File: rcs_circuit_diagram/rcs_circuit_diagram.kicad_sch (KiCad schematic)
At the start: 50 parts, among them J1 Conn_01x06_Pin, J11 Conn_01x02_Pin, J13 Conn_01x02_Pin, J15 Conn_01x02_Pin, J3 Conn_01x02_Pin, J5 Conn_01x02_Pin, J6 Conn_01x02_Pin, J7 Conn_01x02_Pin, J9 Conn_01x02_Pin, U1 LM2596S-5

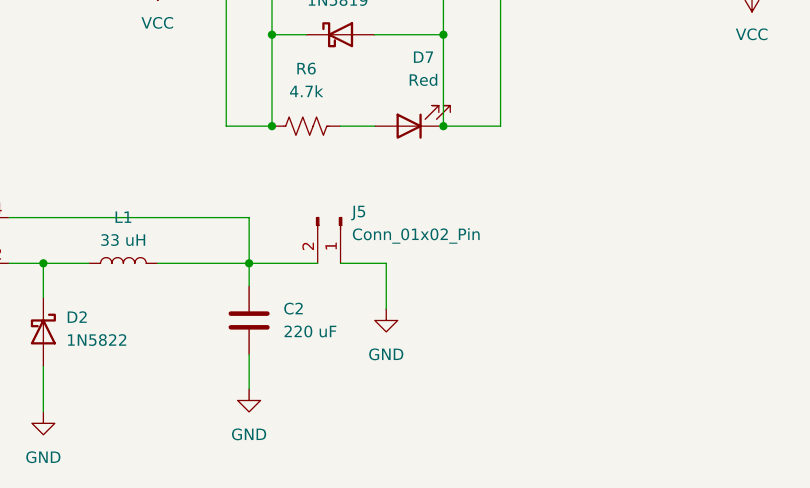
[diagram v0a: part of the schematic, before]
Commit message: Fixed power connection
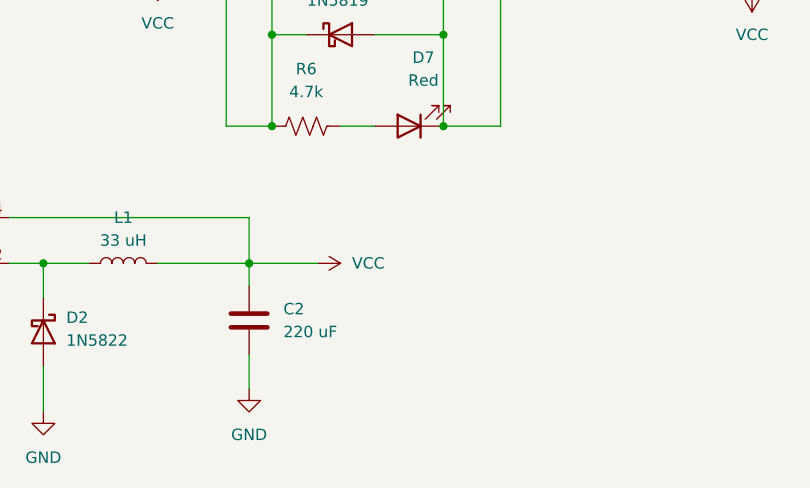
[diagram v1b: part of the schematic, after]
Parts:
- removed J5: Conn_01x02_Pin, symbol Connector:Conn_01x02_Pin
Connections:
- net VCC: now also C2.1, L1.2, U1.4 (FB)
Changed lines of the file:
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@@
-    (stroke (width 0) (type default))
-  )
-  (wire (pts (xy 223.52 229.87) (xy 223.52 234.95))
     (stroke (width 0) (type default))
   )
@@
   )
   (wire (pts (xy 292.1 93.98) (xy 364.49 93.98))
-    (stroke (width 0) (type default))
-  )
-  (wire (pts (xy 218.44 229.87) (xy 223.52 229.87))
     (stroke (width 0) (type default))
   )
@@
     )
   )
-  (symbol (lib_id "power:GND") (at 223.52 234.95 0) (unit 1)
-    (in_bom yes) (on_board yes) (dnp no) (fields_autoplaced)
-    (property "Reference" "#PWR013" (at 223.52 241.3 0)
-      (effects (font (size 1.27 1.27)) hide)
-    )
-    (property "Value" "GND" (at 223.52 240.03 0)
-      (effects (font (size 1.27 1.27)))
-    )
-    (property "Footprint" "" (at 223.52 234.95 0)
-      (effects (font (size 1.27 1.27)) hide)
-    )
-    (property "Datasheet" "" (at 223.52 234.95 0)
-      (effects (font (size 1.27 1.27)) hide)
-    )
-    (pin "1")
-    (instances
-      (project "rcs_circuit_diagram"
-        (path "/c5cfa2cd-8217-4cc7-84bd-4a928cc21c13"
-          (reference "#PWR013") (unit 1)
-        )
-      )
-    )
-  )
   (symbol (lib_id "power:GND") (at 207.01 110.49 0) (unit 1)
     (in_bom yes) (on_board yes) (dnp no) (fields_autoplaced)
@@
         (path "/c5cfa2cd-8217-4cc7-84bd-4a928cc21c13"
           (reference "#PWR032") (unit 1)
+        )
+      )
+    )
+  )
+  (symbol (lib_id "power:VCC") (at 215.9 229.87 270) (unit 1)
+    (in_bom yes) (on_board yes) (dnp no) (fields_autoplaced)
+    (property "Reference" "#PWR013" (at 212.09 229.87 0)
+      (effects (font (size 1.27 1.27)) hide)
+    )
+    (property "Value" "VCC" (at 219.71 229.87 90)
+      (effects (font (size 1.27 1.27)) (justify left))
+    )
+    (property "Footprint" "" (at 215.9 229.87 0)
+      (effects (font (size 1.27 1.27)) hide)
+    )
+    (property "Datasheet" "" (at 215.9 229.87 0)
+      (effects (font (size 1.27 1.27)) hide)
+    )
+    (pin "1")
+    (instances
+      (project "rcs_circuit_diagram"
+        (path "/c5cfa2cd-8217-4cc7-84bd-4a928cc21c13"
+          (reference "#PWR013") (unit 1)
         )
       )
@@
         )
       )
-    )
-  )
-  (symbol (lib_id "Connector:Conn_01x02_Pin") (at 218.44 224.79 270) (unit 1)
-    (in_bom yes) (on_board yes) (dnp no) (fields_autoplaced)
-    (property "Reference" "J5" (at 219.71 224.155 90)
-      (effects (font (size 1.27 1.27)) (justify left))
-    )
-    (property "Value" "Conn_01x02_Pin" (at 219.71 226.695 90)
-      (effects (font (size 1.27 1.27)) (justify left))
-    )
-    (property "Footprint" "" (at 218.44 224.79 0)
-      (effects (font (size 1.27 1.27)) hide)
-    )
-    (property "Datasheet" "~" (at 218.44 224.79 0)
-      (effects (font (size 1.27 1.27)) hide)
-    )
-    (pin "1")
-    (pin "2")
-    (instances
-      (project "rcs_circuit_diagram"
-        (path "/c5cfa2cd-8217-4cc7-84bd-4a928cc21c13"
-          (reference "J5") (unit 1)
-        )
-      )

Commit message: Update rcs_circuit_diagram.kicad_sch
Added footprints
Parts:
- C1, C2: footprint (none) -> Capacitor_SMD:C_0402_1005Metric
- D1, D3, D4, D5, D6, D7: footprint (none) -> LED_SMD:LED_0603_1608Metric
- J1: footprint (none) -> Connector_PinHeader_2.54mm:PinHeader_1x06_P2.54mm_Vertical
- J11, J13, J15, J3, J6, J7, J9: footprint (none) -> Connector_PinHeader_2.54mm:PinHeader_1x02_P2.54mm_Vertical
- L1: footprint (none) -> Inductor_SMD:L_0603_1608Metric
- R1, R2, R3, R4, R5, R6: footprint (none) -> Resistor_SMD:R_0402_1005Metric
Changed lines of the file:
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@@
       (effects (font (size 1.27 1.27)))
     )
-    (property "Footprint" "" (at 214.884 213.614 90)
+    (property "Footprint" "Resistor_SMD:R_0402_1005Metric" (at 214.884 213.614 90)
       (effects (font (size 1.27 1.27)) hide)
     )
@@
       (effects (font (size 1.27 1.27)))
     )
-    (property "Footprint" "" (at 105.664 209.804 90)
+    (property "Footprint" "Resistor_SMD:R_0402_1005Metric" (at 105.664 209.804 90)
       (effects (font (size 1.27 1.27)) hide)
     )
@@
       (effects (font (size 1.27 1.27)) (justify left))
     )
-    (property "Footprint" "" (at 144.4752 236.22 0)
+    (property "Footprint" "Capacitor_SMD:C_0402_1005Metric" (at 144.4752 236.22 0)
       (effects (font (size 1.27 1.27)) hide)
     )
@@
       (effects (font (size 1.27 1.27)) (justify left))
     )
-    (property "Footprint" "" (at 284.48 190.5 0)
+    (property "Footprint" "Connector_PinHeader_2.54mm:PinHeader_1x02_P2.54mm_Vertical" (at 284.48 190.5 0)
       (effects (font (size 1.27 1.27)) hide)
     )
@@
       (effects (font (size 1.27 1.27)))
     )
-    (property "Footprint" "" (at 349.25 148.59 0)
+    (property "Footprint" "LED_SMD:LED_0603_1608Metric" (at 349.25 148.59 0)
       (effects (font (size 1.27 1.27)) hide)
     )
@@
       (effects (font (size 1.27 1.27)) (justify left))
     )
-    (property "Footprint" "" (at 218.44 189.23 0)
+    (property "Footprint" "Connector_PinHeader_2.54mm:PinHeader_1x02_P2.54mm_Vertical" (at 218.44 189.23 0)
       (effects (font (size 1.27 1.27)) hide)
     )
@@
       (effects (font (size 1.27 1.27)))
     )
-    (property "Footprint" "" (at 226.06 214.63 0)
+    (property "Footprint" "LED_SMD:LED_0603_1608Metric" (at 226.06 214.63 0)
       (effects (font (size 1.27 1.27)) hide)
     )
@@
       (effects (font (size 1.27 1.27)))
     )
-    (property "Footprint" "" (at 120.65 210.82 0)
+    (property "Footprint" "LED_SMD:LED_0603_1608Metric" (at 120.65 210.82 0)
       (effects (font (size 1.27 1.27)) hide)
     )
@@
       (effects (font (size 1.27 1.27)))
     )
-    (property "Footprint" "" (at 212.344 147.574 90)
+    (property "Footprint" "Resistor_SMD:R_0402_1005Metric" (at 212.344 147.574 90)
       (effects (font (size 1.27 1.27)) hide)
     )
@@
       (effects (font (size 1.27 1.27)))
     )
-    (property "Footprint" "" (at 194.31 229.87 0)
+    (property "Footprint" "Inductor_SMD:L_0603_1608Metric" (at 194.31 229.87 0)
       (effects (font (size 1.27 1.27)) hide)
     )
@@
       (effects (font (size 1.27 1.27)))
     )
-    (property "Footprint" "" (at 119.634 143.764 90)
+    (property "Footprint" "Resistor_SMD:R_0402_1005Metric" (at 119.634 143.764 90)
       (effects (font (size 1.27 1.27)) hide)
     )
@@
       (effects (font (size 1.27 1.27)))
     )
-    (property "Footprint" "" (at 41.91 125.73 0)
+    (property "Footprint" "Connector_PinHeader_2.54mm:PinHeader_1x06_P2.54mm_Vertical" (at 41.91 125.73 0)
       (effects (font (size 1.27 1.27)) hide)
     )
@@
       (effects (font (size 1.27 1.27)))
     )
-    (property "Footprint" "" (at 43.18 144.78 0)
+    (property "Footprint" "Connector_PinHeader_2.54mm:PinHeader_1x02_P2.54mm_Vertical" (at 43.18 144.78 0)
       (effects (font (size 1.27 1.27)) hide)
     )
@@
       (effects (font (size 1.27 1.27)))
     )
-    (property "Footprint" "" (at 223.52 148.59 0)
+    (property "Footprint" "LED_SMD:LED_0603_1608Metric" (at 223.52 148.59 0)
       (effects (font (size 1.27 1.27)) hide)
     )
@@
       (effects (font (size 1.27 1.27)))
     )
-    (property "Footprint" "" (at 280.924 214.884 90)
+    (property "Footprint" "Resistor_SMD:R_0402_1005Metric" (at 280.924 214.884 90)
       (effects (font (size 1.27 1.27)) hide)
     )
@@
       (effects (font (size 1.27 1.27)) (justify left))
     )
-    (property "Footprint" "" (at 209.2452 240.03 0)
+    (property "Footprint" "Capacitor_SMD:C_0402_1005Metric" (at 209.2452 240.03 0)
       (effects (font (size 1.27 1.27)) hide)
     )
@@
       (effects (font (size 1.27 1.27)) (justify left))
     )
-    (property "Footprint" "" (at 113.03 185.42 0)
+    (property "Footprint" "Connector_PinHeader_2.54mm:PinHeader_1x02_P2.54mm_Vertical" (at 113.03 185.42 0)
       (effects (font (size 1.27 1.27)) hide)
     )
@@
       (effects (font (size 1.27 1.27)))
     )
-    (property "Footprint" "" (at 338.074 147.574 90)
+    (property "Footprint" "Resistor_SMD:R_0402_1005Metric" (at 338.074 147.574 90)
       (effects (font (size 1.27 1.27)) hide)
     )
@@
       (effects (font (size 1.27 1.27)))
     )
-    (property "Footprint" "" (at 130.81 144.78 0)
+    (property "Footprint" "LED_SMD:LED_0603_1608Metric" (at 130.81 144.78 0)
       (effects (font (size 1.27 1.27)) hide)
     )
@@
       (effects (font (size 1.27 1.27)) (justify left))
     )
-    (property "Footprint" "" (at 215.9 123.19 0)
+    (property "Footprint" "Connector_PinHeader_2.54mm:PinHeader_1x02_P2.54mm_Vertical" (at 215.9 123.19 0)
       (effects (font (size 1.27 1.27)) hide)
     )
@@
       (effects (font (size 1.27 1.27)) (justify left))
     )
-    (property "Footprint" "" (at 341.63 123.19 0)
+    (property "Footprint" "Connector_PinHeader_2.54mm:PinHeader_1x02_P2.54mm_Vertical" (at 341.63 123.19 0)
       (effects (font (size 1.27 1.27)) hide)
     )
@@
       (effects (font (size 1.27 1.27)))
     )
-    (property "Footprint" "" (at 292.1 215.9 0)
+    (property "Footprint" "LED_SMD:LED_0603_1608Metric" (at 292.1 215.9 0)
       (effects (font (size 1.27 1.27)) hide)
     )
@@
       (effects (font (size 1.27 1.27)) (justify left))
     )
-    (property "Footprint" "" (at 123.19 119.38 0)
-      (effects (font (size 1.27 1.27)) hide)
-    )
+    (property "Footprint" "Connector_PinHeader_2.54mm:PinHeader_1x02_P2.54mm_Vertical" (at 123.19 119.38 0)
+      (effects (font (size 1.27 1.27)) hide)
+    )

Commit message: Updated footprints, changed layout of components
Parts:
- removed C1: 680 uF, Capacitor_SMD:C_0402_1005Metric, symbol Device:C
- added C3: C_Polarized, Capacitor_THT:CP_Radial_D10.0mm_P2.50mm, symbol Device:C_Polarized
- MOSFET1, MOSFET10, MOSFET11, MOSFET12, MOSFET13, MOSFET14, MOSFET15, MOSFET16, MOSFET17, MOSFET18, MOSFET2, MOSFET3, MOSFET4, MOSFET5, MOSFET6, MOSFET7, MOSFET8, MOSFET9: footprint Package_TO_SOT_THT:TO-220-3_Vertical -> Package_TO_SOT_THT:TO-220-3_Horizontal_TabDown
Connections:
- net GND: now also C3.2
- net VCC: now also C3.1
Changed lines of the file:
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@@
       (effects (font (size 1.27 1.27)) (justify left))
     )
-    (property "Footprint" "Package_TO_SOT_THT:TO-220-3_Vertical" (at 186.69 107.315 0)
+    (property "Footprint" "Package_TO_SOT_THT:TO-220-3_Horizontal_TabDown" (at 186.69 107.315 0)
       (effects (font (size 1.27 1.27) italic) (justify left) hide)
     )
@@
       (effects (font (size 1.27 1.27)) (justify left))
     )
-    (property "Footprint" "Package_TO_SOT_THT:TO-220-3_Vertical" (at 129.54 170.815 0)
+    (property "Footprint" "Package_TO_SOT_THT:TO-220-3_Horizontal_TabDown" (at 129.54 170.815 0)
       (effects (font (size 1.27 1.27) italic) (justify left) hide)
     )
@@
       (effects (font (size 1.27 1.27)) (justify left))
     )
-    (property "Footprint" "Package_TO_SOT_THT:TO-220-3_Vertical" (at 135.89 104.775 0)
+    (property "Footprint" "Package_TO_SOT_THT:TO-220-3_Horizontal_TabDown" (at 135.89 104.775 0)
       (effects (font (size 1.27 1.27) italic) (justify left) hide)
     )
@@
       (effects (font (size 1.27 1.27)) (justify left))
     )
-    (property "Footprint" "Package_TO_SOT_THT:TO-220-3_Vertical" (at 318.77 108.585 0)
+    (property "Footprint" "Package_TO_SOT_THT:TO-220-3_Horizontal_TabDown" (at 318.77 108.585 0)
       (effects (font (size 1.27 1.27) italic) (justify left) hide)
     )
@@
     )
   )
-  (symbol (lib_id "Device:C") (at 143.51 232.41 0) (unit 1)
-    (in_bom yes) (on_board yes) (dnp no) (fields_autoplaced)
-    (property "Reference" "C1" (at 147.32 231.14 0)
-      (effects (font (size 1.27 1.27)) (justify left))
-    )
-    (property "Value" "680 uF" (at 147.32 233.68 0)
-      (effects (font (size 1.27 1.27)) (justify left))
-    )
-    (property "Footprint" "Capacitor_SMD:C_0402_1005Metric" (at 144.4752 236.22 0)
-      (effects (font (size 1.27 1.27)) hide)
-    )
-    (property "Datasheet" "~" (at 143.51 232.41 0)
-      (effects (font (size 1.27 1.27)) hide)
-    )
-    (pin "1")
-    (pin "2")
-    (instances
-      (project "rcs_circuit_diagram"
-        (path "/c5cfa2cd-8217-4cc7-84bd-4a928cc21c13"
-          (reference "C1") (unit 1)
-        )
-      )
-    )
-  )
   (symbol (lib_id "Regulator_Switching:LM2596S-5") (at 168.91 227.33 0) (unit 1)
     (in_bom yes) (on_board yes) (dnp no) (fields_autoplaced)
@@
     )
   )
+  (symbol (lib_id "Device:C_Polarized") (at 143.51 232.41 0) (unit 1)
+    (in_bom yes) (on_board yes) (dnp no) (fields_autoplaced)
+    (property "Reference" "C3" (at 147.32 230.251 0)
+      (effects (font (size 1.27 1.27)) (justify left))
+    )
+    (property "Value" "C_Polarized" (at 147.32 232.791 0)
+      (effects (font (size 1.27 1.27)) (justify left))
+    )
+    (property "Footprint" "Capacitor_THT:CP_Radial_D10.0mm_P2.50mm" (at 144.4752 236.22 0)
+      (effects (font (size 1.27 1.27)) hide)
+    )
+    (property "Datasheet" "~" (at 143.51 232.41 0)
+      (effects (font (size 1.27 1.27)) hide)
+    )
+    (pin "1")
+    (pin "2")
+    (instances
+      (project "rcs_circuit_diagram"
+        (path "/c5cfa2cd-8217-4cc7-84bd-4a928cc21c13"
+          (reference "C3") (unit 1)
+        )
+      )
+    )
+  )
   (symbol (lib_id "Transistor_FET:IRLB8721PBF") (at 284.48 170.18 0) (unit 1)
     (in_bom yes) (on_board yes) (dnp no) (fields_autoplaced)
@@
       (effects (font (size 1.27 1.27)) (justify left))
     )
-    (property "Footprint" "Package_TO_SOT_THT:TO-220-3_Vertical" (at 290.83 172.085 0)
+    (property "Footprint" "Package_TO_SOT_THT:TO-220-3_Horizontal_TabDown" (at 290.83 172.085 0)
       (effects (font (size 1.27 1.27) italic) (justify left) hide)
     )
@@
       (effects (font (size 1.27 1.27)) (justify left))
     )
-    (property "Footprint" "Package_TO_SOT_THT:TO-220-3_Vertical" (at 241.3 107.315 0)
+    (property "Footprint" "Package_TO_SOT_THT:TO-220-3_Horizontal_TabDown" (at 241.3 107.315 0)
       (effects (font (size 1.27 1.27) italic) (justify left) hide)
     )
@@
       (effects (font (size 1.27 1.27)) (justify left))
     )
-    (property "Footprint" "Package_TO_SOT_THT:TO-220-3_Vertical" (at 295.91 108.585 0)
+    (property "Footprint" "Package_TO_SOT_THT:TO-220-3_Horizontal_TabDown" (at 295.91 108.585 0)
       (effects (font (size 1.27 1.27) italic) (justify left) hide)
     )
@@
       (effects (font (size 1.27 1.27)) (justify left))
     )
-    (property "Footprint" "Package_TO_SOT_THT:TO-220-3_Vertical" (at 210.82 107.315 0)
+    (property "Footprint" "Package_TO_SOT_THT:TO-220-3_Horizontal_TabDown" (at 210.82 107.315 0)
       (effects (font (size 1.27 1.27) italic) (justify left) hide)
     )
@@
       (effects (font (size 1.27 1.27)) (justify left))
     )
-    (property "Footprint" "Package_TO_SOT_THT:TO-220-3_Vertical" (at 101.6 170.815 0)
+    (property "Footprint" "Package_TO_SOT_THT:TO-220-3_Horizontal_TabDown" (at 101.6 170.815 0)
       (effects (font (size 1.27 1.27) italic) (justify left) hide)
     )
@@
       (effects (font (size 1.27 1.27)) (justify left))
     )
-    (property "Footprint" "Package_TO_SOT_THT:TO-220-3_Vertical" (at 115.57 104.775 0)
+    (property "Footprint" "Package_TO_SOT_THT:TO-220-3_Horizontal_TabDown" (at 115.57 104.775 0)
       (effects (font (size 1.27 1.27) italic) (justify left) hide)
     )
@@
       (effects (font (size 1.27 1.27)) (justify left))
     )
-    (property "Footprint" "Package_TO_SOT_THT:TO-220-3_Vertical" (at 179.07 174.625 0)
+    (property "Footprint" "Package_TO_SOT_THT:TO-220-3_Horizontal_TabDown" (at 179.07 174.625 0)
       (effects (font (size 1.27 1.27) italic) (justify left) hide)
     )
@@
       (effects (font (size 1.27 1.27)) (justify left))
     )
-    (property "Footprint" "Package_TO_SOT_THT:TO-220-3_Vertical" (at 320.04 172.085 0)
+    (property "Footprint" "Package_TO_SOT_THT:TO-220-3_Horizontal_TabDown" (at 320.04 172.085 0)
       (effects (font (size 1.27 1.27) italic) (justify left) hide)
     )
@@
       (effects (font (size 1.27 1.27)) (justify left))
     )
-    (property "Footprint" "Package_TO_SOT_THT:TO-220-3_Vertical" (at 236.22 174.625 0)
+    (property "Footprint" "Package_TO_SOT_THT:TO-220-3_Horizontal_TabDown" (at 236.22 174.625 0)
       (effects (font (size 1.27 1.27) italic) (justify left) hide)
     )
@@
       (effects (font (size 1.27 1.27)) (justify left))
     )
-    (property "Footprint" "Package_TO_SOT_THT:TO-220-3_Vertical" (at 347.98 172.085 0)
+    (property "Footprint" "Package_TO_SOT_THT:TO-220-3_Horizontal_TabDown" (at 347.98 172.085 0)
       (effects (font (size 1.27 1.27) italic) (justify left) hide)
     )
@@
       (effects (font (size 1.27 1.27)) (justify left))
     )
-    (property "Footprint" "Package_TO_SOT_THT:TO-220-3_Vertical" (at 72.39 170.815 0)
+    (property "Footprint" "Package_TO_SOT_THT:TO-220-3_Horizontal_TabDown" (at 72.39 170.815 0)
       (effects (font (size 1.27 1.27) italic) (justify left) hide)
     )
@@
       (effects (font (size 1.27 1.27)) (justify left))
     )
-    (property "Footprint" "Package_TO_SOT_THT:TO-220-3_Vertical" (at 346.71 108.585 0)
+    (property "Footprint" "Package_TO_SOT_THT:TO-220-3_Horizontal_TabDown" (at 346.71 108.585 0)
       (effects (font (size 1.27 1.27) italic) (justify left) hide)
     )
@@
       (effects (font (size 1.27 1.27)) (justify left))
     )
-    (property "Footprint" "Package_TO_SOT_THT:TO-220-3_Vertical" (at 86.36 104.775 0)
+    (property "Footprint" "Package_TO_SOT_THT:TO-220-3_Horizontal_TabDown" (at 86.36 104.775 0)
       (effects (font (size 1.27 1.27) italic) (justify left) hide)
     )
@@
       (effects (font (size 1.27 1.27)) (justify left))
     )
-    (property "Footprint" "Package_TO_SOT_THT:TO-220-3_Vertical" (at 208.28 174.625 0)
-      (effects (font (size 1.27 1.27) italic) (justify left) hide)
-    )
+    (property "Footprint" "Package_TO_SOT_THT:TO-220-3_Horizontal_TabDown" (at 208.28 174.625 0)
+      (effects (font (size 1.27 1.27) italic) (justify left) hide)
+    )

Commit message: Everything is very much not right
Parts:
- added J2: Conn_01x02_Pin, Connector_PinHeader_2.54mm:PinHeader_1x02_P2.54mm_Vertical, symbol Connector:Conn_01x02_Pin
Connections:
- net GND: now also J2.2 (Pin_2)
- net VCC: no longer C2.1, L1.2, U1.4 (FB)
- new net: C2.1, J2.1 (Pin_1), L1.2, U1.4 (FB)
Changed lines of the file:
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@@
     (stroke (width 0) (type default))
   )
-  (wire (pts (xy 208.28 229.87) (xy 215.9 229.87))
+  (wire (pts (xy 208.28 229.87) (xy 227.33 229.87))
     (stroke (width 0) (type default))
   )
@@
   )
   (wire (pts (xy 208.28 229.87) (xy 208.28 232.41))
+    (stroke (width 0) (type default))
+  )
+  (wire (pts (xy 227.33 227.33) (xy 227.33 223.52))
     (stroke (width 0) (type default))
   )
@@
     )
   )
+  (symbol (lib_id "power:GND") (at 227.33 223.52 180) (unit 1)
+    (in_bom yes) (on_board yes) (dnp no) (fields_autoplaced)
+    (property "Reference" "#PWR033" (at 227.33 217.17 0)
+      (effects (font (size 1.27 1.27)) hide)
+    )
+    (property "Value" "GND" (at 227.33 218.44 0)
+      (effects (font (size 1.27 1.27)))
+    )
+    (property "Footprint" "" (at 227.33 223.52 0)
+      (effects (font (size 1.27 1.27)) hide)
+    )
+    (property "Datasheet" "" (at 227.33 223.52 0)
+      (effects (font (size 1.27 1.27)) hide)
+    )
+    (pin "1")
+    (instances
+      (project "rcs_circuit_diagram"
+        (path "/c5cfa2cd-8217-4cc7-84bd-4a928cc21c13"
+          (reference "#PWR033") (unit 1)
+        )
+      )
+    )
+  )
   (symbol (lib_id "Regulator_Switching:LM2596S-5") (at 168.91 227.33 0) (unit 1)
     (in_bom yes) (on_board yes) (dnp no) (fields_autoplaced)
@@
         (path "/c5cfa2cd-8217-4cc7-84bd-4a928cc21c13"
           (reference "#PWR032") (unit 1)
-        )
-      )
-    )
-  )
-  (symbol (lib_id "power:VCC") (at 215.9 229.87 270) (unit 1)
-    (in_bom yes) (on_board yes) (dnp no) (fields_autoplaced)
-    (property "Reference" "#PWR013" (at 212.09 229.87 0)
-      (effects (font (size 1.27 1.27)) hide)
-    )
-    (property "Value" "VCC" (at 219.71 229.87 90)
-      (effects (font (size 1.27 1.27)) (justify left))
-    )
-    (property "Footprint" "" (at 215.9 229.87 0)
-      (effects (font (size 1.27 1.27)) hide)
-    )
-    (property "Datasheet" "" (at 215.9 229.87 0)
-      (effects (font (size 1.27 1.27)) hide)
-    )
-    (pin "1")
-    (instances
-      (project "rcs_circuit_diagram"
-        (path "/c5cfa2cd-8217-4cc7-84bd-4a928cc21c13"
-          (reference "#PWR013") (unit 1)
         )
       )
@@
         )
       )
+    )
+  )
+  (symbol (lib_id "Connector:Conn_01x02_Pin") (at 232.41 229.87 180) (unit 1)
+    (in_bom yes) (on_board yes) (dnp no) (fields_autoplaced)
+    (property "Reference" "J2" (at 231.775 234.95 0)
+      (effects (font (size 1.27 1.27)) hide)
+    )
+    (property "Value" "Conn_01x02_Pin" (at 231.775 232.41 0)
+      (effects (font (size 1.27 1.27)))
+    )
+    (property "Footprint" "Connector_PinHeader_2.54mm:PinHeader_1x02_P2.54mm_Vertical" (at 232.41 229.87 0)
+      (effects (font (size 1.27 1.27)) hide)
+    )
+    (property "Datasheet" "~" (at 232.41 229.87 0)
+      (effects (font (size 1.27 1.27)) hide)
+    )
+    (pin "1")
+    (pin "2")
+    (instances
+      (project "rcs_circuit_diagram"
+        (path "/c5cfa2cd-8217-4cc7-84bd-4a928cc21c13"
+          (reference "J2") (unit 1)
+        )
+      )
